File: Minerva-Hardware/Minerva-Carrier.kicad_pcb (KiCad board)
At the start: 4 copper layers, 83.5 x 90 mm, 175 parts, among them J1 HDMI_D_1.4, J14 JST_SHBM04B-SRSS-TB, J20 SPK_1.25mm_4P, J21 SPK_1.25mm_4P, J22 AUX_IN_3.5mm, J23 USB-C 24P (C5156605), J24 BATT JST-PH 2P, J25 FACEPLATE 14P, J3 Bus_M.2_Socket_B, J4 Bus_M.2_Socket_M, J5 Conn_01x22_Female, J6 THD-02-R, J7 JAE_SIM_Card_SF72S006, J8 THD-20-R, M6 M.2 Solder Nut, M7 M.2 Screw, SW1 Right angle Tact button, U1 BQ25798, U2 ASEK-32.768KHZ-L-R-T, U20 SN65DSI86ZQER, U21 HD3SS460RHRT, U22 TPS65987DDJRSHR, U23 W25Q32JVSS, U24 AP2112K-1.8, U25 AP2112K-1.2, U29 PAM8406DR, U30 TPS61088RHLR, U31 MAX17048G+T10, U6 AP22653W6, U8 AP3441SHE-7B

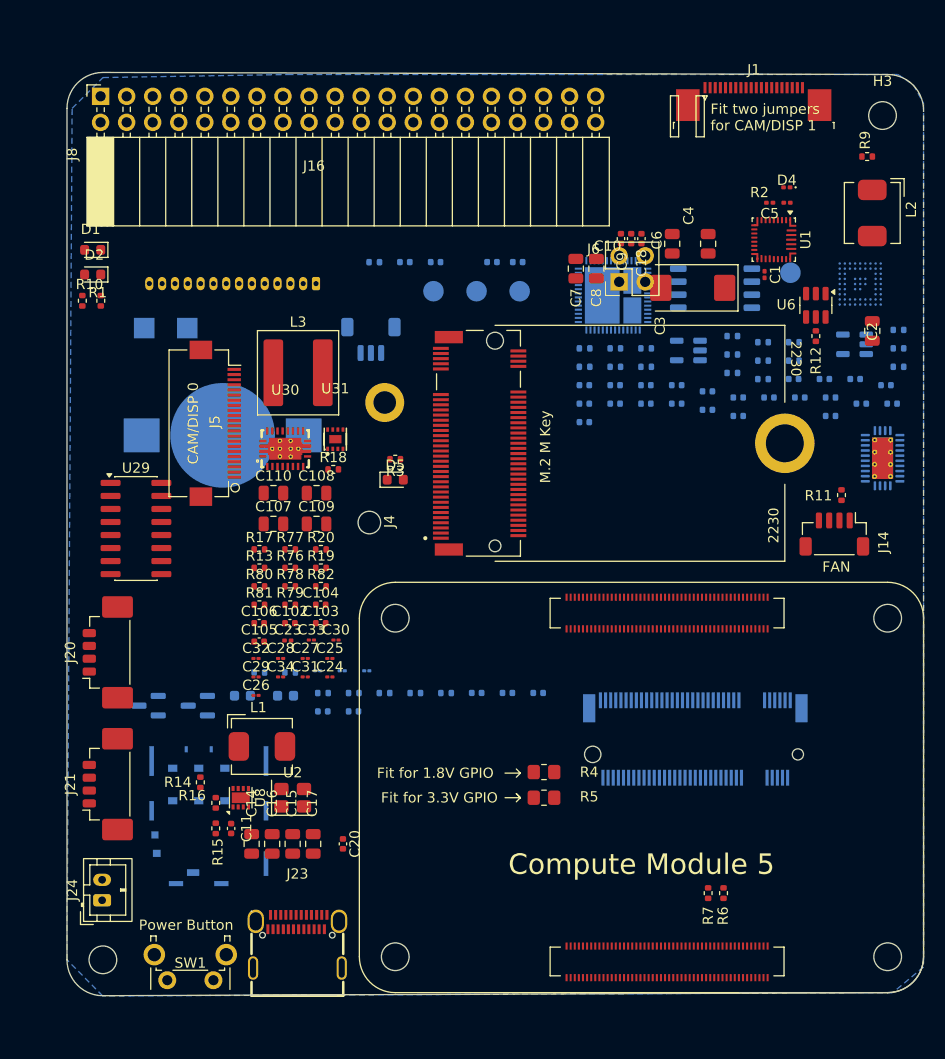
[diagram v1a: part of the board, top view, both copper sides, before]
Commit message: hardware: snapshot carrier and face-board integration
Hardware schematics and power:
- complete the BQ25798 charger, TPS61088 5 V boost, MAX17048 gauge, battery controls, and cross-sheet power hierarchy
- add the SN65DSI86 display bridge, HD3SS460 mux, TPS65987D PD controller, USB-C protection, M.2 support, and corrected named-interface wiring
- move the Core2350B0 onto the face-board interconnect, route controls through J25/J2, and make Select directly assert nRPIBOOT
- remove the obsolete J6/J8 expansion headers and move J23 USB-C to the carrier top-left with its VBUS switch and charger support cluster

PCB, footprints, and mechanical assets:
- establish the six-layer controlled-impedance carrier stack, net classes, HDI rules, ground/power planes, keepouts, and placed carrier floorplan
- add the routed two-layer Minerva-Face board with eleven controls, four M2.5 holes, interconnects, fiducials, and a 3.5-inch display datum
- add corrected project-local footprints and STEP models for Core2350B0, USB-C, bridge/PD/power ICs, PicoBlade connectors, M.2 hardware, and critical mechanical envelopes
- correct BAT54 pin mapping, TPS61088 thermal-via numbering, J23 shell geometry, and board-edge lug rules

Verification and reference material:
- add sourcing evidence, ERC/DRC artifacts, STEP assemblies, face render, mechanical coordinates, controlled-impedance notes, and strict connectivity checklists
- document the dock architecture and current board-to-board pin contract
- remove transient root-level DRC and netlist dumps

Torchform and workstation integration:
- fix four-column home navigation and add controller focus/adjustment for quick-settings volume and brightness sliders
- configure Kitty as the terminal backend and add the Minerva SSH workspace folder

Known work-in-progress at this snapshot:
- carrier schematic/PCB parity is clean, but routing remains incomplete at 499 unconnected items with 53 differential-pair tuning violations
- the face board is DRC-clean and f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
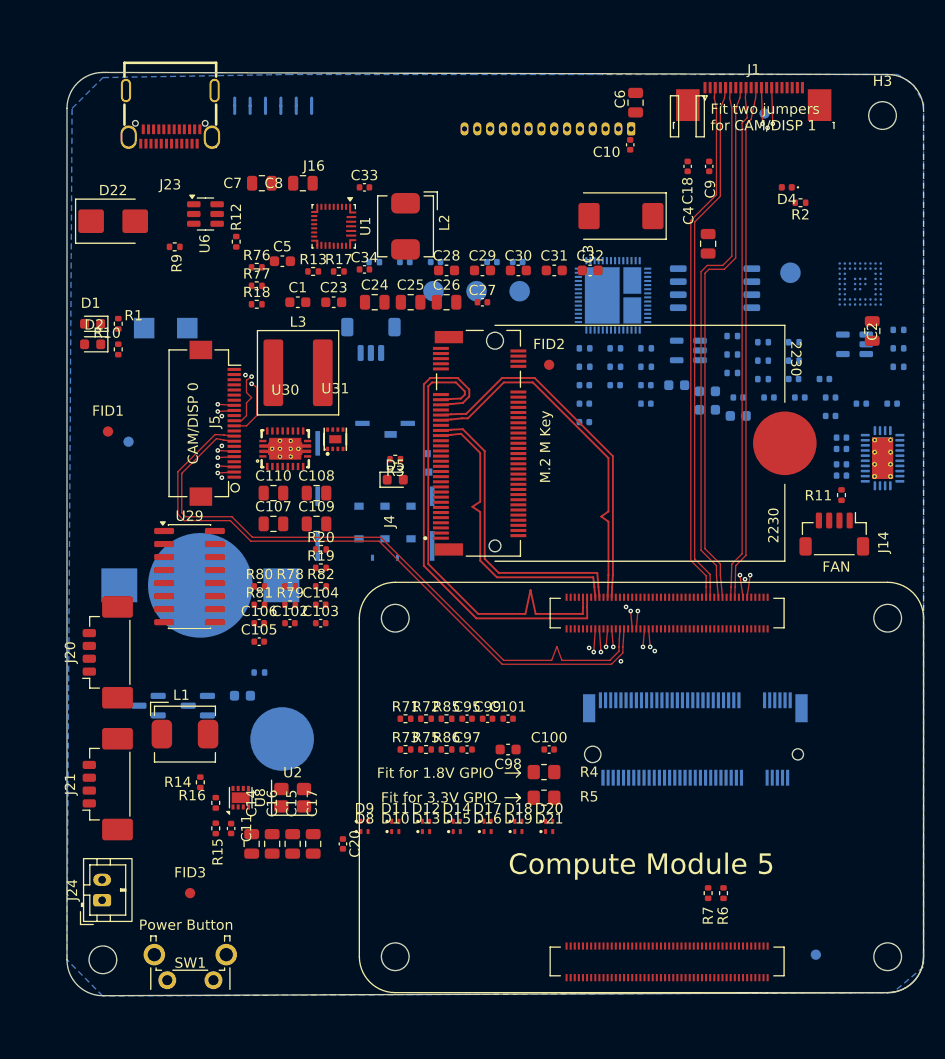
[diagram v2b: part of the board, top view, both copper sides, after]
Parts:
- removed C19: 0.1uF, Capacitor_SMD:C_01005_0402Metric
- removed C21, C22: 10uF, Capacitor_SMD:C_01005_0402Metric
- removed J6: THD-02-R, Connector_PinHeader_2.54mm:PinHeader_2x02_P2.54mm_Vertical
- removed J8: THD-20-R, Connector_PinSocket_2.54mm:PinSocket_2x20_P2.54mm_Horizontal
- removed M7: M.2 Screw, MountingHole_2.2mm_M2
- added D10: TPD1E01B04DPYR, Package_SON:Texas_DPY0002A_0.6x1mm_P0.65mm, F.Cu at (111.0, 144.0)
- added D11: TPD1E01B04DPYR, Package_SON:Texas_DPY0002A_0.6x1mm_P0.65mm, F.Cu at (111.0, 143.0)
- added D12: TPD1E01B04DPYR, Package_SON:Texas_DPY0002A_0.6x1mm_P0.65mm, F.Cu at (114.0, 143.0)
- added D13: TPD1E01B04DPYR, Package_SON:Texas_DPY0002A_0.6x1mm_P0.65mm, F.Cu at (114.0, 144.0)
- added D14: TPD1E01B04DPYR, Package_SON:Texas_DPY0002A_0.6x1mm_P0.65mm, F.Cu at (117.0, 143.0)
- added D15: TPD1E01B04DPYR, Package_SON:Texas_DPY0002A_0.6x1mm_P0.65mm, F.Cu at (117.0, 144.0)
- added D16: TPD1E05U06DPYR, Package_SON:Texas_DPY0002A_0.6x1mm_P0.65mm, F.Cu at (120.0, 144.0)
- added D17: TPD1E05U06DPYR, Package_SON:Texas_DPY0002A_0.6x1mm_P0.65mm, F.Cu at (120.0, 143.0)
- added D18: TPD1E05U06DPYR, Package_SON:Texas_DPY0002A_0.6x1mm_P0.65mm, F.Cu at (123.0, 143.0)
- added D19: TPD1E05U06DPYR, Package_SON:Texas_DPY0002A_0.6x1mm_P0.65mm, F.Cu at (123.0, 144.0)
- added D20: TPD1E05U06DPYR, Package_SON:Texas_DPY0002A_0.6x1mm_P0.65mm, F.Cu at (126.0, 143.0)
- added D21: TPD1E05U06DPYR, Package_SON:Texas_DPY0002A_0.6x1mm_P0.65mm, F.Cu at (126.0, 144.0)
- added D22: SMBJ24CA, Diode_SMD:D_SMB, F.Cu at (83.5, 84.5)
- added D8: TPD1E01B04DPYR, Package_SON:Texas_DPY0002A_0.6x1mm_P0.65mm, F.Cu at (108.0, 144.0)
- added D9: TPD1E01B04DPYR, Package_SON:Texas_DPY0002A_0.6x1mm_P0.65mm, F.Cu at (108.0, 143.0)
- added FID1: Fiducial_1mm_Mask2mm, Fiducial_1mm_Mask2mm, F.Cu at (83.0, 105.0)
- added FID2: Fiducial_1mm_Mask2mm, Fiducial_1mm_Mask2mm, F.Cu at (126.0, 98.5)
- added FID3: Fiducial_1mm_Mask2mm, Fiducial_1mm_Mask2mm, F.Cu at (91.0, 150.0)
- added FID4: Fiducial_1mm_Mask2mm, Fiducial_1mm_Mask2mm, B.Cu at (85.0, 106.0)
- added FID5: Fiducial_1mm_Mask2mm, Fiducial_1mm_Mask2mm, B.Cu at (147.0, 74.0)
- added FID6: Fiducial_1mm_Mask2mm, Fiducial_1mm_Mask2mm, B.Cu at (152.0, 156.0)
- C1, C23, C5: footprint Capacitor_SMD:C_0201_0603Metric -> C_0603_1608Metric
- C100, C101, C95, C97, C98, C99, R71, R72, R73, R75, R85, R86: moved to F.Cu
- C12, C13: value C -> 100nF
- C24, C25, C26: footprint Capacitor_SMD:C_01005_0402Metric -> C_0805_2012Metric
- C27, C33, C34: footprint Capacitor_SMD:C_01005_0402Metric -> C_0402_1005Metric
- C28, C29, C30, C31, C32: footprint Capacitor_SMD:C_01005_0402Metric -> C_0603_1608Metric
- C75, C76, C82, C83: footprint C_0402_1005Metric -> C_0603_1608Metric
- D4: footprint LED_SMD:LED_0201_0603Metric -> LED_0402_1005Metric
- M6: value M.2 Solder Nut -> 2x M.2 Card Standoff; footprint MountingHole_2.2mm_M2_DIN965_Pad -> Minerva:SMTSO-M2-4ET
- R2: footprint Resistor_SMD:R_0201_0603Metric -> R_0402_1005Metric
- moved J23 81.3 mm to (89.1, 74.4), turned to 180 degrees
- moved R9 68.1 mm to (89.5, 87.0), turned to 0 degrees
- moved U6 60.2 mm to (92.5, 83.8), turned to 0 degrees
- moved R12 57.2 mm to (95.5, 86.5), turned to 90 degrees
- moved C32 49.9 mm to (130.0, 89.3)
- moved C5 47.8 mm to (100.0, 88.4), turned to 0 degrees
- moved C31 46.5 mm to (126.5, 89.3)
- moved C1 45.6 mm to (101.5, 92.4), turned to 0 degrees
- moved L2 45.5 mm to (112.0, 85.0)
- moved C29 45.4 mm to (119.5, 89.3)
- moved C33 44.4 mm to (108.0, 81.2)
- moved U1 42.9 mm to (105.0, 85.0)
- moved C26 42.6 mm to (116.0, 92.4)
- moved C28 41.1 mm to (116.0, 89.3)
- moved C34 40.6 mm to (108.0, 89.2)
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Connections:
- J4 pad M1: unconnected-(J4-GND2230-PadM1) -> GND
- M6 pad 1: (no net) -> GND
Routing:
- net /CM5_HighSpeed/DPHY0_D3_N: track 0.00 -> 66.3 mm, vias 0 -> 2
- net /CM5_HighSpeed/DPHY0_D3_P: track 0.00 -> 66.3 mm, vias 0 -> 2
- net /CM5_HighSpeed/DPHY0_D1_P: track 0.00 -> 64.0 mm, vias 0 -> 2
- net /CM5_HighSpeed/DPHY0_D1_N: track 0.00 -> 63.6 mm, vias 0 -> 2
- net /CM5_HighSpeed/DPHY0_C_N: track 0.00 -> 63.4 mm
- net /CM5_HighSpeed/DPHY0_C_P: track 0.00 -> 63.4 mm
- net /CM5_HighSpeed/DPHY0_D0_N: track 0.00 -> 58.0 mm, vias 0 -> 2
- net /CM5_HighSpeed/DPHY0_D0_P: track 0.00 -> 58.0 mm, vias 0 -> 2
- net /CM5_HighSpeed/DPHY0_D2_N: track 0.00 -> 56.6 mm, vias 0 -> 2
- net /CM5_HighSpeed/DPHY0_D2_P: track 0.00 -> 56.4 mm, vias 0 -> 2
- net /CM5_HighSpeed/HDMI_D1_N: track 0.00 -> 52.5 mm
- net /CM5_HighSpeed/HDMI_D1_P: track 0.00 -> 52.5 mm
- net /CM5_HighSpeed/HDMI_D2_N: track 0.00 -> 51.4 mm
- net /CM5_HighSpeed/HDMI_D2_P: track 0.00 -> 51.4 mm
- net /CM5_HighSpeed/HDMI_CLK_N: track 0.00 -> 50.9 mm, vias 0 -> 2
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- added copper zone on In4.Cu, net /+5v
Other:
- copper layers 4 -> 6
- rule solder_mask_min_width: 4 -> 0.1
